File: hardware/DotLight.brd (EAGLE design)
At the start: 25.4 x 45.7 mm, 23 parts, among them Q1 BSH103, Q2 BSH103

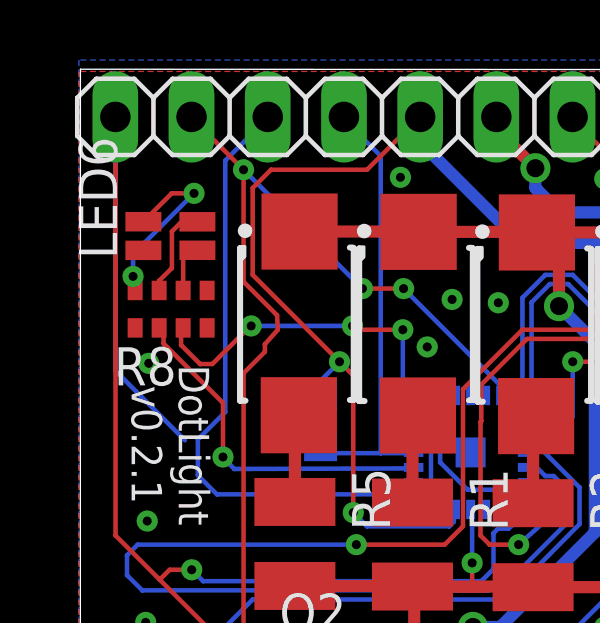
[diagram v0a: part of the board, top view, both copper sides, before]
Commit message: Rearrange logos
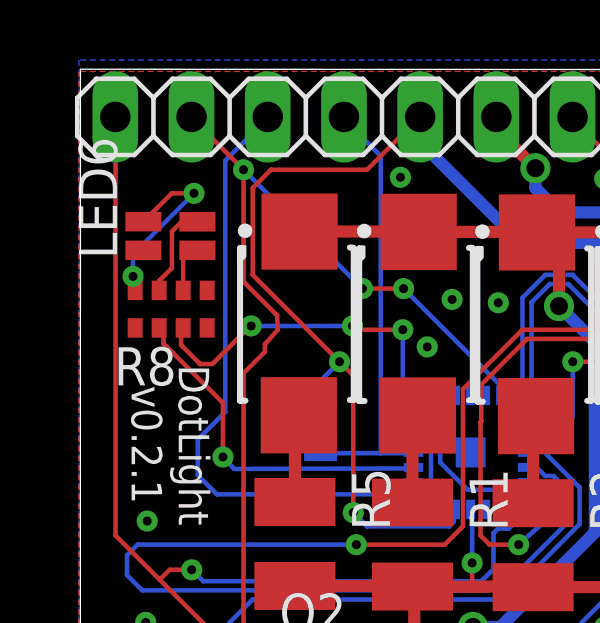
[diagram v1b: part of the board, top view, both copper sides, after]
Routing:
- net MOSI: track 54.4 -> 42.8 mm
- net TOUCH_EMIT: vias 22 -> 21
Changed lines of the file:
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@@
 <layer number="18" name="Vias" color="2" fill="1" visible="yes" active="yes"/>
 <layer number="19" name="Unrouted" color="6" fill="1" visible="no" active="yes"/>
-<layer number="20" name="Dimension" color="15" fill="1" visible="yes" active="yes"/>
-<layer number="21" name="tPlace" color="7" fill="1" visible="no" active="yes"/>
-<layer number="22" name="bPlace" color="7" fill="1" visible="yes" active="yes"/>
+<layer number="20" name="Dimension" color="15" fill="1" visible="no" active="yes"/>
+<layer number="21" name="tPlace" color="7" fill="1" visible="yes" active="yes"/>
+<layer number="22" name="bPlace" color="7" fill="1" visible="no" active="yes"/>
 <layer number="23" name="tOrigins" color="15" fill="1" visible="no" active="yes"/>
 <layer number="24" name="bOrigins" color="15" fill="1" visible="no" active="yes"/>
@@
 <dimension x1="24.00611875" y1="32.03465" x2="23.95785625" y2="0.820390625" x3="39.385971875" y3="16.4037" textsize="1.778" layer="48"/>
 <dimension x1="0.380475" y1="0.79325" x2="25.8120625" y2="0.80006875" x3="13.098325" y3="-6.87395" textsize="1.778" layer="48"/>
-<text x="3.2427625" y="24.14508125" size="0.8128" layer="22" rot="MR180">12.2017</text>
-<text x="2.4484" y="25.589459375" size="0.8128" layer="22" rot="MR180">Mihai Galos</text>
+<text x="2.4045625" y="24.11968125" size="0.8128" layer="22" rot="MR180">12.2017</text>
+<text x="1.4324" y="25.589459375" size="0.8128" layer="22" rot="MR180">Mihai Galos</text>
 <rectangle x1="22.95" y1="0.84" x2="25.24" y2="2.2" layer="29"/>
 <rectangle x1="0.8923" y1="22.8563" x2="1.3749" y2="22.8817" layer="21" rot="R90"/>
@@
 <wire x1="15.0876" y1="32.1564" x2="13.716" y2="32.1564" width="0.1524" layer="16"/>
 <wire x1="15.24" y1="32.004" x2="15.0876" y2="32.1564" width="0.1524" layer="16"/>
-<wire x1="1.9812" y1="44.5008" x2="1.9812" y2="36.1188" width="0.1524" layer="16"/>
+<wire x1="1.9812" y1="44.5008" x2="1.9812" y2="36.1188" width="0" layer="19" extent="1-16"/>
 <wire x1="12.8016" y1="35.2044" x2="12.8176" y2="35.301" width="0.1524" layer="16"/>
 <wire x1="1.9812" y1="44.5008" x2="1.974715625" y2="44.58476875" width="0.1524" layer="16"/>
@@
 <wire x1="14.5796" y1="30.7086" x2="14.5796" y2="29.5148" width="0.1524" layer="16"/>
 <wire x1="14.5796" y1="29.5148" x2="14.1732" y2="29.1084" width="0.1524" layer="16"/>
-<wire x1="1.9812" y1="36.1188" x2="4.2926" y2="33.8074" width="0.1524" layer="16"/>
+<wire x1="1.9812" y1="36.1188" x2="4.2926" y2="33.8074" width="0" layer="19" extent="1-16"/>
 <wire x1="14.1732" y1="29.1084" x2="4.9022" y2="29.1084" width="0.1524" layer="16"/>
 <wire x1="4.9022" y1="29.1084" x2="4.5212" y2="29.4894" width="0.1524" layer="16"/>
@@
 <wire x1="17.4498" y1="31.0134" x2="14.9606" y2="28.4988" width="0.1524" layer="16"/>
 <via x="3.0372" y="31.1136" extent="1-16" drill="0.3"/>
-<via x="3.088" y="36.3714" extent="1-16" drill="0.3"/>
+<wire x1="3.088" y1="36.3714" x2="3.088" y2="36.3714" width="0" layer="19" extent="1-16"/>
 </signal>
 <signal name="TOUCH_SENSE">

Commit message: Add R to RGB
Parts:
- moved LOGO1 1.40 mm to (13.4, 13.1)
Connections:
- new net RED: R8.1, U$1.11
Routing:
- net RED: track 0.00 -> 13.1 mm, vias 0 -> 1
- net SCK: track 23.2 -> 24.4 mm, vias 0 -> 2
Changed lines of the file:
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@@
 <layer number="17" name="Pads" color="2" fill="1" visible="yes" active="yes"/>
 <layer number="18" name="Vias" color="2" fill="1" visible="yes" active="yes"/>
-<layer number="19" name="Unrouted" color="6" fill="1" visible="no" active="yes"/>
+<layer number="19" name="Unrouted" color="6" fill="1" visible="yes" active="yes"/>
 <layer number="20" name="Dimension" color="15" fill="1" visible="no" active="yes"/>
 <layer number="21" name="tPlace" color="7" fill="1" visible="yes" active="yes"/>
 <layer number="22" name="bPlace" color="7" fill="1" visible="no" active="yes"/>
-<layer number="23" name="tOrigins" color="15" fill="1" visible="no" active="yes"/>
+<layer number="23" name="tOrigins" color="15" fill="1" visible="yes" active="yes"/>
 <layer number="24" name="bOrigins" color="15" fill="1" visible="no" active="yes"/>
 <layer number="25" name="tNames" color="7" fill="1" visible="no" active="yes"/>
@@
 <wire x1="26.234921875" y1="46.160209375" x2="26.229840625" y2="14.696390625" width="0" layer="20"/>
 <dimension x1="-8.26314375" y1="2.548390625" x2="-8.26314375" y2="30.488390625" x3="-3.18314375" y3="16.518390625" textsize="1.778" layer="48"/>
-<text x="3.024871875" y="33.6540375" size="1.016" layer="21" rot="SR270" align="center">v0.2.1</text>
+<text x="13.3359625" y="11.000471875" size="1.016" layer="21" rot="SR0" align="center">v0.2.1</text>
 <dimension x1="24.00611875" y1="32.03465" x2="23.95785625" y2="0.820390625" x3="39.385971875" y3="16.4037" textsize="1.778" layer="48"/>
 <dimension x1="0.380475" y1="0.79325" x2="25.8120625" y2="0.80006875" x3="13.098325" y3="-6.87395" textsize="1.778" layer="48"/>
@@
 <rectangle x1="10.8745" y1="20.6719" x2="11.6111" y2="20.6973" layer="21" rot="R90"/>
 <rectangle x1="11.0777" y1="20.6719" x2="11.4587" y2="20.6973" layer="21" rot="R90"/>
-<text x="4.0862" y="36.3198" size="1.016" layer="21" rot="SR270">DotLight</text>
+<text x="10.086" y="15.1098" size="1.016" layer="21" rot="SR0">DotLight</text>
 <wire x1="19.3308" y1="0.4636" x2="7.2308" y2="0.4636" width="0" layer="20"/>
 <wire x1="7.2308" y1="0.4636" x2="7.23" y2="14.6736" width="0" layer="20"/>
@@
 <element name="LED5" library="HighPowerLed" package="LUXEON_5630" value="LUXEON_5630" x="8.04" y="37.69" rot="R270"/>
 <element name="R5" library="resistor" package="R1210" value="12Ω 0.5W" x="7.96" y="30.35" rot="R270"/>
-<element name="LOGO1" library="Particle-Devices" package="OSHW-LOGO-S" value="OSHW-LOGOS" x="13.2894" y="11.6812"/>
+<element name="LOGO1" library="Particle-Devices" package="OSHW-LOGO-S" value="OSHW-LOGOS" x="13.3656" y="13.0782"/>
 <element name="JP3" library="Spark" package="USB-A-PCB" value="USBPCB" x="13.29" y="5.47" rot="R90"/>
 <element name="JP4" library="pinhead" package="1X03" value="" x="21.98" y="16.26" rot="R180"/>
@@
 <wire x1="15.0876" y1="32.1564" x2="13.716" y2="32.1564" width="0.1524" layer="16"/>
 <wire x1="15.24" y1="32.004" x2="15.0876" y2="32.1564" width="0.1524" layer="16"/>
-<wire x1="1.9812" y1="44.5008" x2="1.9812" y2="36.1188" width="0" layer="19" extent="1-16"/>
 <wire x1="12.8016" y1="35.2044" x2="12.8176" y2="35.301" width="0.1524" layer="16"/>
 <wire x1="1.9812" y1="44.5008" x2="1.974715625" y2="44.58476875" width="0.1524" layer="16"/>
@@
 <wire x1="14.5796" y1="30.7086" x2="14.5796" y2="29.5148" width="0.1524" layer="16"/>
 <wire x1="14.5796" y1="29.5148" x2="14.1732" y2="29.1084" width="0.1524" layer="16"/>
-<wire x1="1.9812" y1="36.1188" x2="4.2926" y2="33.8074" width="0" layer="19" extent="1-16"/>
 <wire x1="14.1732" y1="29.1084" x2="4.9022" y2="29.1084" width="0.1524" layer="16"/>
 <wire x1="4.9022" y1="29.1084" x2="4.5212" y2="29.4894" width="0.1524" layer="16"/>
@@
 <wire x1="12.4968" y1="32.1564" x2="12.4968" y2="33.6804" width="0.1524" layer="16"/>
 <wire x1="12.3444" y1="32.004" x2="12.4968" y2="32.1564" width="0.1524" layer="16"/>
-<wire x1="5.3594" y1="32.004" x2="12.3444" y2="32.004" width="0.1524" layer="16"/>
+<wire x1="5.6388" y1="32.004" x2="12.3444" y2="32.004" width="0.1524" layer="16"/>
 <wire x1="7.0104" y1="44.5008" x2="5.6388" y2="43.1292" width="0.1524" layer="16"/>
 <wire x1="12.0396" y1="33.8328" x2="11.9176" y2="33.901" width="0.1524" layer="16"/>
 <wire x1="7.0104" y1="44.5008" x2="7.054715625" y2="44.58476875" width="0.1524" layer="16"/>
 <wire x1="5.6388" y1="34.7472" x2="5.6388" y2="43.1292" width="0.1524" layer="16"/>
-<wire x1="5.6388" y1="34.7472" x2="4.7244" y2="33.8328" width="0.1524" layer="16"/>
-<wire x1="4.7244" y1="33.8328" x2="4.7244" y2="32.639" width="0.1524" layer="16"/>
-<wire x1="4.7244" y1="32.639" x2="5.3594" y2="32.004" width="0.1524" layer="16"/>
+<wire x1="5.6388" y1="32.004" x2="5.334" y2="31.6992" width="0.1524" layer="16"/>
+<via x="5.334" y="31.6992" extent="1-16" drill="0.3"/>
+<wire x1="5.334" y1="31.6992" x2="4.9276" y2="31.6992" width="0.1524" layer="1"/>
+<wire x1="4.9276" y1="31.6992" x2="4.572" y2="32.0548" width="0.1524" layer="1"/>
+<wire x1="4.572" y1="32.0548" x2="4.572" y2="34.3662" width="0.1524" layer="1"/>
+<wire x1="4.572" y1="34.3662" x2="4.8514" y2="34.6456" width="0.1524" layer="1"/>
+<via x="4.8514" y="34.6456" extent="1-16" drill="0.3"/>
+<wire x1="4.8514" y1="34.6456" x2="5.5372" y2="34.6456" width="0.1524" layer="16"/>
+<wire x1="5.5372" y1="34.6456" x2="5.6388" y2="34.7472" width="0.1524" layer="16"/>
 </signal>
 <signal name="RXD">
@@
 <via x="25.113259375" y="25.555259375" extent="1-16" drill="0.3"/>
 <via x="18.255259375" y="11.196640625" extent="1-16" drill="0.3"/>
-<via x="13.309878125" y="15.303821875" extent="1-16" drill="0.3"/>
+<via x="13.335278125" y="16.802421875" extent="1-16" drill="0.3"/>
 <via x="7.2261375" y="15.651021875" extent="1-16" drill="0.3"/>
 <via x="11.47788125" y="42.571621875" extent="1-16" drill="0.3"/>
@@
 <wire x1="17.4498" y1="32.2326" x2="17.4498" y2="31.0134" width="0.1524" layer="16"/>
 <wire x1="17.4498" y1="31.0134" x2="14.9606" y2="28.4988" width="0.1524" layer="16"/>
-<via x="3.0372" y="31.1136" extent="1-16" drill="0.3"/>
-<wire x1="3.088" y1="36.3714" x2="3.088" y2="36.3714" width="0" layer="19" extent="1-16"/>
+<via x="2.8086" y="31.1136" extent="1-16" drill="0.3"/>
 </signal>
 <signal name="TOUCH_SENSE">
@@
 <wire x1="3.5814" y1="37.4052" x2="3.4354" y2="37.5512" width="0.1524" layer="1"/>
 </signal>
+<signal name="RED">
+<contactref element="U$1" pad="11"/>
+<contactref element="R8" pad="1"/>
+<wire x1="11.9176" y1="32.401" x2="5.6642" y2="32.401" width="0.1524" layer="16"/>
+<wire x1="5.6642" y1="32.401" x2="5.6642" y2="32.4104" width="0.1524" layer="16"/>
+<wire x1="5.6642" y1="32.4104" x2="4.9022" y2="32.4104" width="0.1524" layer="16"/>
+<wire x1="4.9022" y1="32.4104" x2="2.6416" y2="34.671" width="0.1524" layer="16"/>
+<wire x1="2.6416" y1="34.671" x2="2.6416" y2="36.4744" width="0.1524" layer="16"/>
+<wire x1="2.6416" y1="36.4744" x2="2.667" y2="36.4998" width="0.1524" layer="16"/>
+<via x="2.667" y="36.4998" extent="1-16" drill="0.3"/>
+<wire x1="2.667" y1="36.4998" x2="2.667" y2="37.5196" width="0.1524" layer="1"/>
+<wire x1="2.667" y1="37.5196" x2="2.6354" y2="37.5512" width="0.1524" layer="1"/>
+</signal>
 </signals>

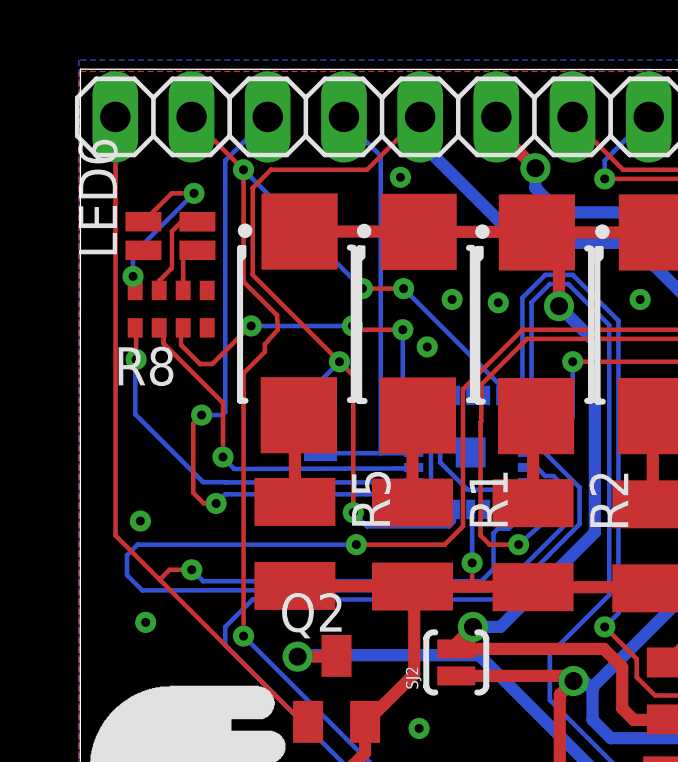
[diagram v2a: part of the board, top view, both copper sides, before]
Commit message: Correct RGB 3V3
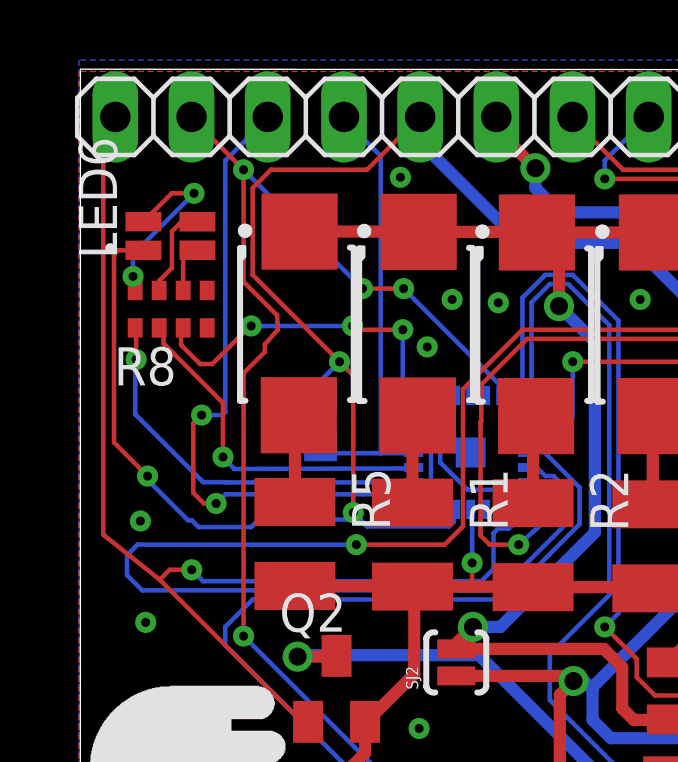
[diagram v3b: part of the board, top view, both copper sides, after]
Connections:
- net VIN_PIN: now also LED6.4
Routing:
- net VIN_PIN: track 95.1 -> 111.9 mm, vias 4 -> 5
- net MOSI: track 42.8 -> 43.4 mm
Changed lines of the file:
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@@
 <layer number="18" name="Vias" color="2" fill="1" visible="yes" active="yes"/>
 <layer number="19" name="Unrouted" color="6" fill="1" visible="yes" active="yes"/>
-<layer number="20" name="Dimension" color="15" fill="1" visible="no" active="yes"/>
+<layer number="20" name="Dimension" color="15" fill="1" visible="yes" active="yes"/>
 <layer number="21" name="tPlace" color="7" fill="1" visible="yes" active="yes"/>
 <layer number="22" name="bPlace" color="7" fill="1" visible="no" active="yes"/>
@@
 <text x="14.7574" y="7.747" size="1.016" layer="22" rot="MR0">&lt;5s</text>
 <text x="14.732" y="2.6924" size="1.016" layer="22" rot="MR0">&gt;5s</text>
+<circle x="1.8034" y="40.2082" radius="0.091578125" width="0.1524" layer="21"/>
 </plain>
 <attributes>
@@
 <wire x1="1.9812" y1="44.5008" x2="1.974715625" y2="44.58476875" width="0.1524" layer="16"/>
 <wire x1="8.0772" y1="24.5364" x2="8.382" y2="24.5364" width="0.1524" layer="1"/>
-<wire x1="1.9812" y1="30.6324" x2="3.4544" y2="29.1592" width="0.1524" layer="1"/>
+<wire x1="1.5748" y1="30.6578" x2="3.4544" y2="29.1592" width="0.1524" layer="1"/>
 <wire x1="3.4544" y1="29.1592" x2="8.0772" y2="24.5364" width="0.1524" layer="1"/>
-<wire x1="1.9812" y1="44.5008" x2="1.9812" y2="30.6324" width="0.1524" layer="1"/>
+<wire x1="1.5748" y1="44.5262" x2="1.5748" y2="30.6578" width="0.1524" layer="1"/>
 <wire x1="8.382" y1="24.5364" x2="8.4" y2="24.42" width="0.1524" layer="1"/>
-<wire x1="1.9812" y1="44.5008" x2="1.974715625" y2="44.58476875" width="0.1524" layer="1"/>
+<wire x1="1.5748" y1="44.5262" x2="1.974715625" y2="44.58476875" width="0.1524" layer="1"/>
 <wire x1="15.24" y1="32.004" x2="15.24" y2="31.0134" width="0.1524" layer="16"/>
 <wire x1="15.24" y1="31.0134" x2="15.0876" y2="30.861" width="0.1524" layer="16"/>
@@
 <wire x1="8.816340625" y1="35.31018125" x2="8.60933125" y2="35.31018125" width="0.1524" layer="16"/>
 <wire x1="8.60933125" y1="35.31018125" x2="8.60933125" y2="35.58413125" width="0.1524" layer="16"/>
+<contactref element="LED6" pad="4"/>
+<wire x1="2.91" y1="40.1371" x2="2.0625" y2="40.1371" width="0.1524" layer="1"/>
+<wire x1="2.0625" y1="40.1371" x2="1.9304" y2="40.005" width="0.1524" layer="1"/>
+<wire x1="1.9304" y1="40.005" x2="1.9304" y2="33.7312" width="0.1524" layer="1"/>
+<wire x1="1.9304" y1="33.7312" x2="3.048" y2="32.6136" width="0.1524" layer="1"/>
+<via x="3.048" y="32.6136" extent="1-16" drill="0.3"/>
+<wire x1="3.048" y1="32.6136" x2="3.048" y2="32.4866" width="0.1524" layer="16"/>
+<wire x1="3.048" y1="32.4866" x2="4.3942" y2="31.1404" width="0.1524" layer="16"/>
+<wire x1="4.3942" y1="31.1404" x2="4.5212" y2="31.1404" width="0.1524" layer="16"/>
+<wire x1="4.5212" y1="31.1404" x2="4.7498" y2="30.9118" width="0.1524" layer="16"/>
+<wire x1="4.7498" y1="30.9118" x2="6.5024" y2="30.9118" width="0.1524" layer="16"/>
+<wire x1="6.5024" y1="30.9118" x2="6.7564" y2="31.1658" width="0.1524" layer="16"/>
+<wire x1="6.7564" y1="31.1658" x2="9.6774" y2="31.1658" width="0.1524" layer="16"/>
+<wire x1="9.6774" y1="31.1658" x2="9.906" y2="31.3944" width="0.1524" layer="16"/>
 </signal>
 <signal name="RST">
